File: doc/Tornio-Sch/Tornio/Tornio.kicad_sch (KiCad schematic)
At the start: 0 parts

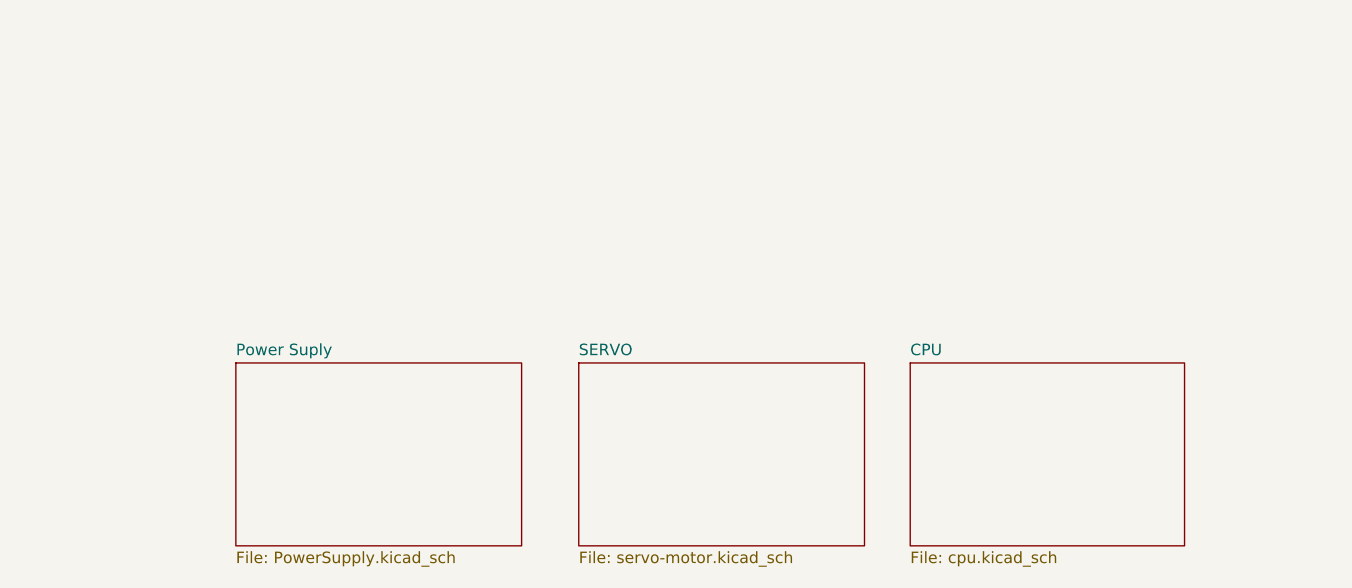
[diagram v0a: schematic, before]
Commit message: spindle protection
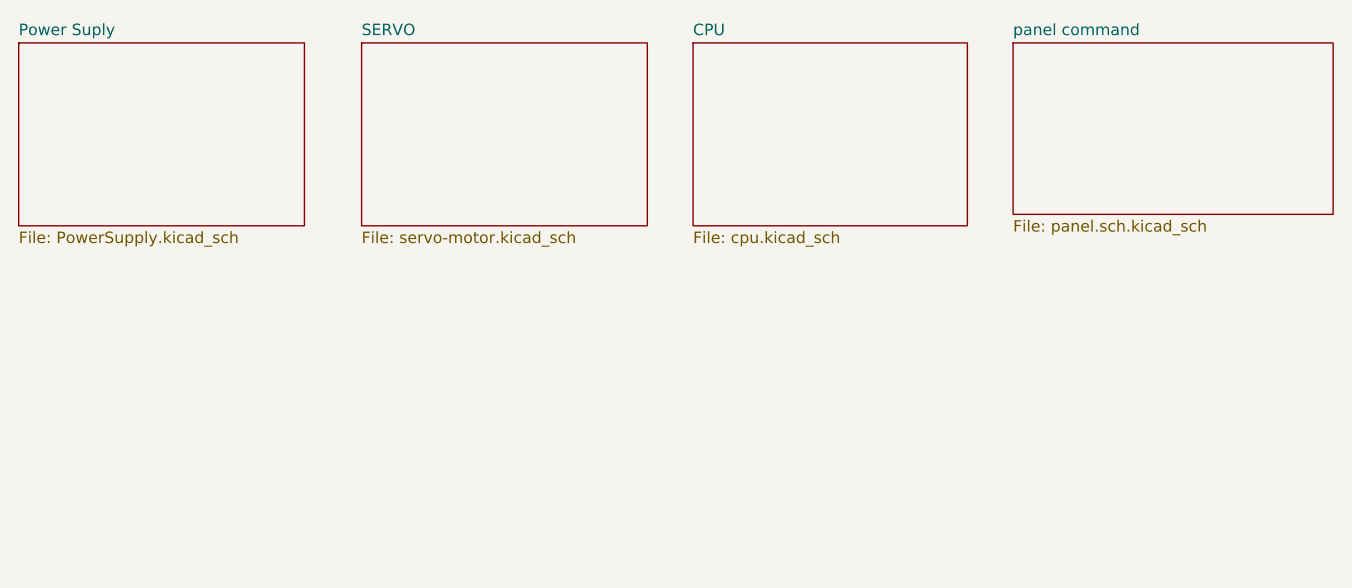
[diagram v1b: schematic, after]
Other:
- added sheet panel command (panel.sch.kicad_sch)
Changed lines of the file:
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@@
 (kicad_sch
-	(version 20240812)
+	(version 20250114)
 	(generator "eeschema")
-	(generator_version "8.99")
+	(generator_version "9.0")
 	(paper "A4")
 	(title_block
@@
 	)
 	(sheet
-		(at 85.09 60.96)
+		(at 133.35 25.4)
+		(size 35.56 19.05)
+		(exclude_from_sim no)
+		(in_bom yes)
+		(on_board yes)
+		(dnp no)
+		(fields_autoplaced yes)
+		(stroke
+			(width 0.1524)
+			(type solid)
+		)
+		(fill
+			(color 0 0 0 0.0000)
+		)
+		(property "Sheetname" "panel command"
+			(at 133.35 24.6884 0)
+			(effects
+				(font
+					(size 1.27 1.27)
+				)
+				(justify left bottom)
+			)
+		)
+		(property "Sheetfile" "panel.sch.kicad_sch"
+			(at 133.35 45.0346 0)
+			(effects
+				(font
+					(size 1.27 1.27)
+				)
+				(justify left top)
+			)
+		)
+		(instances
+			(project "Tornio"
+				(path "/d482d245-9bde-482f-a0c9-8f57ac89377e"
+					(page "6")
+				)
+			)
+		)
+	)
+	(sheet
+		(at 60.96 25.4)
 		(size 31.75 20.32)
 		(exclude_from_sim no)
@@
 		)
 		(property "Sheetname" "SERVO"
-			(at 85.09 60.2484 0)
+			(at 60.96 24.6884 0)
 			(effects
 				(font
@@
 		)
 		(property "Sheetfile" "servo-motor.kicad_sch"
-			(at 85.09 81.8646 0)
+			(at 60.96 46.3046 0)
 			(effects
 				(font
@@
 	)
 	(sheet
-		(at 121.92 60.96)
+		(at 97.79 25.4)
 		(size 30.48 20.32)
 		(exclude_from_sim no)
@@
 		)
 		(property "Sheetname" "CPU"
-			(at 121.92 60.2484 0)
+			(at 97.79 24.6884 0)
 			(effects
 				(font
@@
 		)
 		(property "Sheetfile" "cpu.kicad_sch"
-			(at 121.92 81.8646 0)
+			(at 97.79 46.3046 0)
 			(effects
 				(font
@@
 	)
 	(sheet
-		(at 46.99 60.96)
+		(at 22.86 25.4)
 		(size 31.75 20.32)
 		(exclude_from_sim no)
@@
 		)
 		(property "Sheetname" "Power Suply"
-			(at 46.99 60.2484 0)
+			(at 22.86 24.6884 0)
 			(effects
 				(font
@@
 		)
 		(property "Sheetfile" "PowerSupply.kicad_sch"
-			(at 46.99 81.8646 0)
+			(at 22.86 46.3046 0)
 			(effects
 				(font

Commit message: 02-2026 - update
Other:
- added sheet Rimbalzo-Segnali (Rimbalzo-Segnali.kicad_sch)
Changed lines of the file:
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@@
+			(project "Tornio"
+				(path "/d482d245-9bde-482f-a0c9-8f57ac89377e"
+					(page "5")
+				)
+			)
+		)
+	)
+	(sheet
+		(at 184.15 25.4)
+		(size 38.1 17.78)
+		(exclude_from_sim no)
+		(in_bom yes)
+		(on_board yes)
+		(dnp no)
+		(fields_autoplaced yes)
+		(stroke
+			(width 0.1524)
+			(type solid)
+		)
+		(fill
+			(color 0 0 0 0.0000)
+		)
+		(property "Sheetname" "Rimbalzo-Segnali"
+			(at 184.15 24.6884 0)
+			(effects
+				(font
+					(size 1.27 1.27)
+				)
+				(justify left bottom)
+			)
+		)
+		(property "Sheetfile" "Rimbalzo-Segnali.kicad_sch"
+			(at 184.15 43.7646 0)
+			(effects
+				(font
+					(size 1.27 1.27)
+				)
+				(justify left top)
+			)
+		)
+		(instances
 			(project "Tornio"
 				(path "/d482d245-9bde-482f-a0c9-8f57ac89377e"

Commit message: accessori
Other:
- sheet CPU renamed CPU -1
- sheet Rimbalzo-Segnali renamed CPU-IN-OUT-INTERFACE
- added sheet CPU-2 (cpu-2_sch.kicad_sch)
- note added: "1"
- note added: "2"
- note added: "3"
- note added: "4"
- note added: "5"
- note added: "6"
- note added: "ASSE X"
- note added: "ASSE Y"
- note added: "ASSE Z"
- note added: "COMMAND PANEL"
- note added: "MORSETTIERA"
- note added: "SPINDLE"
